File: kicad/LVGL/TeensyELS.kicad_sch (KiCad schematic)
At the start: 52 parts, among them J1 RJ45_Shielded, J2 Conn_01x04_Pin, J3 Conn_01x14_Socket, J4 Screw_Terminal_01x02, J5 Conn_02x03_Odd_Even, Q1 BSS138, Q2 BSS138, Q3 BSS138, Q4 BSS138, Q5 BSS138, Q6 BSS138, Q7 BSS138, Q8 BSS138, Q9 BSS138, SW1 SW_Omron_B3FS, SW10 SW_Omron_B3FS, SW2 SW_Omron_B3FS, SW3 SW_Omron_B3FS, SW4 SW_Omron_B3FS, SW5 SW_Omron_B3FS, SW6 SW_Omron_B3FS, SW7 SW_Omron_B3FS, SW8 SW_Omron_B3FS, SW9 SW_Omron_B3FS, U1 AMS1117-3.3, U2 ESP32-WROOM-32E

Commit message: Choose the encoder input type with a jumper, not a soldering iron
R13/R14 were 0R links: fit them and the spindle encoder's A/B arrive straight
on IO34/IO35; leave them off, fit R15/R16 instead, and the signal goes through
the BSS138s. Picking between the two meant a soldering iron and knowing which
of four 0805s in a row did what. J7, an 8-way header, makes it two jumpers.

Which position means what is not readable off the board, so the silkscreen now
carries a legend - the header drawn twice with the shunts shown in place:

* Volt, rows 1 and 3, pads (7,8) and (3,4). Through R16/R15 into the gates of
  Q8/Q1. A 5V or 12V push-pull output must NOT reach IO34/IO35, whose absolute
  maximum is 3.6V; the FETs level-shift it. They also invert it, which for a
  quadrature pair with no index costs nothing - inverting BOTH channels
  preserves which one leads.

* NPN, rows 2 and 4, pads (5,6) and (1,2). Straight through. An open-collector
  output sinks against R18/R17, the 10K pull-ups to +3.3V already on those nets.

FIT ONE SET, NEVER BOTH. With both in on a channel the FET's drain IS the
signal driving its gate, so it shorts the encoder's output to ground every time
that output goes high. The legend draws two whole configurations for exactly
that reason. The old 0R/1K pairs carried the same hazard, but you had to reach
for solder to create it. Note also that the gate is driven through 1K with no
clamp, so "Volt" means up to the BSS138's +/-20V VGS: a 24V encoder is past it.

THE KNOB NOW HAS A BUTTON. E1 pin 3 was unconnected; it goes through R22 (1K)
to IO0, which R20 already pulls to +3.3V, so a press reads about 0.3V. Nothing
in the firmware reads it yet. IO0 is a strapping pin, so holding the knob down
through a reset puts the ESP32 into serial-download mode - a black screen, and
not something firmware can defend against, because the level is latched before
any code runs.

SW1 IS GONE. It shorted the driver side of Q2 to +5V by hand, which is the same
pulse the al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
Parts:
- removed R13, R14: 0K, Resistor_SMD:R_0805_2012Metric, symbol Device:R
- removed SW1: SW_Omron_B3FS, Button_Switch_THT:SW_TH_Tactile_Omron_B3F-10xx, symbol Switch:SW_Omron_B3FS
- added J7: Conn_02x04_Odd_Even, Connector_PinHeader_2.54mm:PinHeader_2x04_P2.54mm_Vertical, symbol Connector_Generic:Conn_02x04_Odd_Even
- added R22: 1K, Resistor_SMD:R_0805_2012Metric, symbol Device:R
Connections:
- net BOOT: now also R22.2
- net EncA: now also J7.6 (Pin_6)
- net EncB: now also J7.2 (Pin_2)
- net at R16.1: now also J7.8 (Pin_8); no longer J2.4 (Pin_4)
- net at J2.3 (Pin_3): now also J7.1 (Pin_1), J7.3 (Pin_3); no longer R15.1
- net at E1.3 (SW): now also R22.1
- new net: J7.4 (Pin_4), R15.1
- new net: J2.4 (Pin_4), J7.5 (Pin_5), J7.7 (Pin_7)
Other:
- moved on the sheet: J2, Q1, Q8, R15, R16, R17, R18

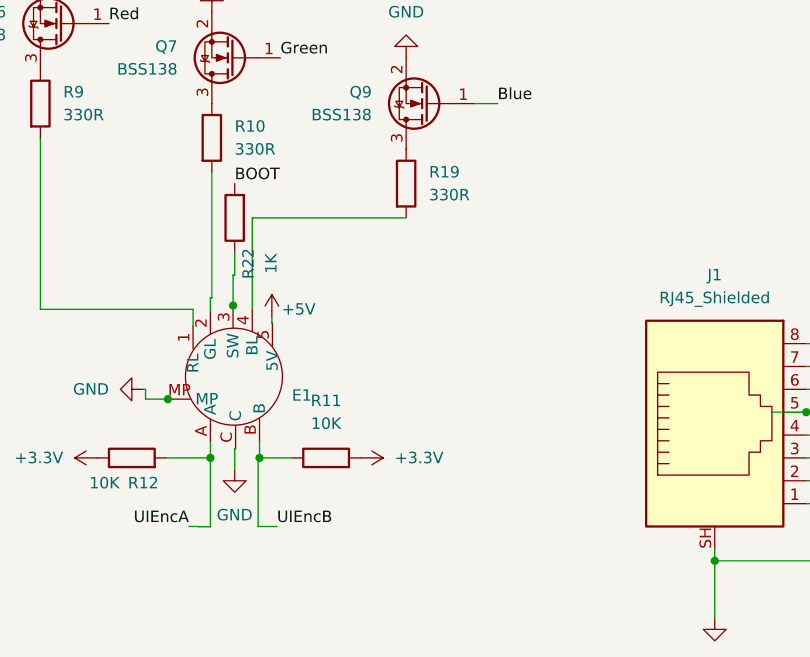
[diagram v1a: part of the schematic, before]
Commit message: The knob switch returns to +5V, so invert it into IO0
1cedd6c wired E1 pin 3 through R22 straight to IO0, on the assumption that the
switch's other terminal was the encoder common, which this board ties to
ground. It is not. It returns to pin 5 - the LED common anode, which sits at
+5V. That commit's account of the circuit is wrong in both directions, and this
corrects it.

WHAT THE COMMITTED CIRCUIT WOULD HAVE DONE. Two failures, neither needing the
other to be fatal:

* IT COULD NOT BE READ. R20 already pulls IO0 to +3.3V, so the pin idles HIGH.
  A press pulls it up as well. Both states are the same state.

* PRESSED WAS OUT OF SPEC. Ignoring the clamp, the node would sit at
  (5/1K + 3.3/10K) / (1/1K + 1/10K) = 4.85V. The ESP32's protection diode pins
  it near 3.9V instead and swallows about 1.1mA into the 3.3V rail. Absolute
  maximum on a GPIO is VDD+0.3 = 3.6V.

The boot warning in that message was backwards too: a press would have held IO0
HIGH, the normal boot level, so it could never have reached download mode.

THE FIX IS THE LEVEL SHIFT THIS BOARD USES EVERYWHERE ELSE. R22 now feeds the
gate of Q10, a BSS138, instead of IO0. R23 (10K) holds that gate down so it
does not float while the switch is open. Q10's source is grounded, its drain is
IO0, and R20 goes on being both the pull-up and the boot strap.

  released   gate at 0V, FET off, IO0 at 3.3V - the level a normal boot needs
  pressed    gate at 4.55V, FET on, IO0 at ~0V

Active low. The gate sits at 4.55V rather than 5V because R22 and R23 divide
it, which is still far above the BSS138's threshold and far below its +/-20V
VGS limit; the switch carries 5V/11K = 455uA.

THE STRAPPING HAZARD IS NOW REAL, where the earlier note only imagined it.
Holding the knob through a reset pulls IO0 low and the ESP32 comes up in serial
download mode - a black screen until it is power-cycled without the knob. That
is ordinary BOOT-button behaviour and it is a deliberate trade, because IO0 is
the only pin left: the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
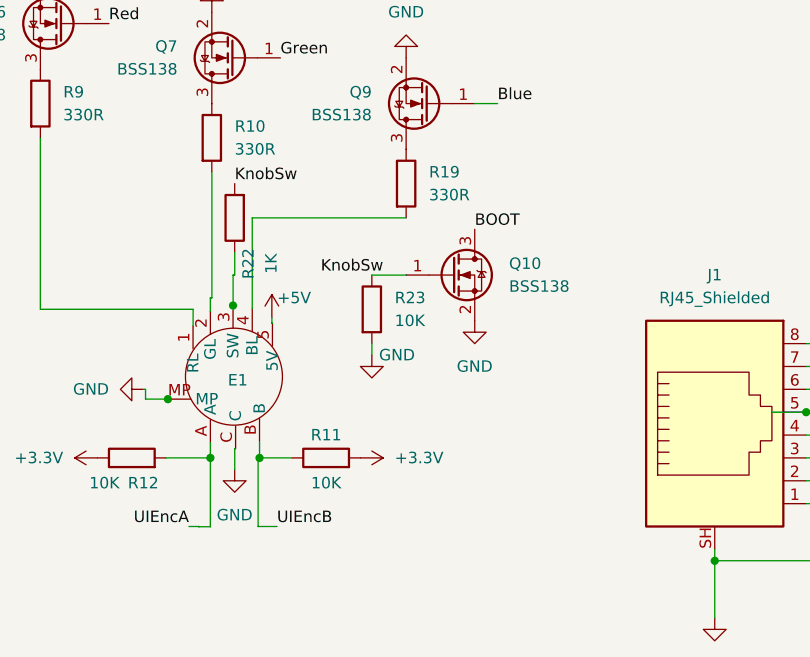
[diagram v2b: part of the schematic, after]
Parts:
- added Q10: BSS138, Package_TO_SOT_SMD:SOT-23, symbol Transistor_FET:BSS138
- added R23: 10K, Resistor_SMD:R_0805_2012Metric, symbol Device:R
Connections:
- net BOOT: now also Q10.3 (D); no longer R22.2
- net GND: now also Q10.2 (S), R23.2
- new net KnobSw: Q10.1 (G), R22.2, R23.1

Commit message: Make the programming header a right-angle part, reachable from the edge
J5 was a vertical SMD header sitting on the board face, which means a
programmer can only be plugged in with the board out. It is now the horizontal
variant, moved from (32.53, 24.21) at -90 to (31.38, 26.95) at 90, so the pins
present at the top board edge: the fab outline reaches y=19.67 against an edge
at y=19.90, i.e. flush with it.

IT IS NO LONGER AN SMD PART. Connector_PinHeader_1.27mm has no horizontal SMD
variant, so this is PinHeader_2x03_P1.27mm_Horizontal - six plated holes,
0.65mm drill on 1.0mm pads, where there were six 2.4x0.74mm SMD pads. That
takes J5 out of the SMT placement step and makes it a through-hole line item.
The committed CPL and position files are a rev behind already and will need
regenerating regardless, but this is now a reason rather than just tidiness.

Nets survived pad for pad: 1 /EN, 2 +3.3V, 3 /TXD, 4 GND, 5 /RXD, 6 /BOOT.

The schematic's Footprint field is set to match here. It had already been
changed in eeschema but not yet saved, so the file on disk still named the
Vertical_SMD part at the moment this was checked; saving afterwards produced
byte-identical content, so the two routes agreed and nothing was lost.
Connectivity is untouched and ERC is unmoved at 63. One general note worth
keeping from the confusion: KiCad's schematic-parity check does NOT compare
footprint identity - it reported clean while the two files named different
parts - so a real sch/pcb footprint mismatch will not be caught by DRC.

ONE NEW DRC ERROR, DELIBERATELY LEFT FOR A DECISION: starved_thermal on J5
pad 2 (+3.3V) against the In2.Cu plane - one thermal spoke where the zone asks
for two, because 1.27mm pitch leaves nowhere to put the second. The pad IS
connected; unconnected items are still zero. The choices are to set that pad's
zone connection to solid, to drop the zone's minimum spoke count, or to waive
it, and which one is right depends on how the board gets assembled. Not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
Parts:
- J5: footprint Connector_PinHeader_1.27mm:PinHeader_2x03_P1.27mm_Vertical_SMD -> Connector_PinHeader_1.27mm:PinHeader_2x03_P1.27mm_Horizontal
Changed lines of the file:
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@@
 			)
 		)
-		(property "Footprint" "Connector_PinHeader_1.27mm:PinHeader_2x03_P1.27mm_Vertical_SMD"
+		(property "Footprint" "Connector_PinHeader_1.27mm:PinHeader_2x03_P1.27mm_Horizontal"
 			(at 339.09 224.79 0)
 			(effects
